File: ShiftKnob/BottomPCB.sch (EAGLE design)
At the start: 37 parts, among them IC2 UA78M05DCY, J1 AVR_SPI_PRG_6PTH, Q1 16MHz, Q2 MOSFET-NCHANNELSMD, Q3 MOSFET-PCHANNELSMD, Q4 MOSFET-NCHANNELSMD, Q5 MOSFET-NCHANNELSMD, Q6 MOSFET-NCHANNELSMD, U1 ATMEGA328, U3 FT232RL-BASICSSOP

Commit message: move silk screens for better visibility.
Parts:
- renumbered U$6 to U6
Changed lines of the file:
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@@
 <part name="GND15" library="SparkFun" deviceset="GND" device=""/>
 <part name="U3" library="SparkFun-DigitalIC" deviceset="FT232RL-BASIC" device="SSOP"/>
-<part name="U$6" library="FORD_frames" deviceset="USB-MINI-B_VERTICAL" device=""/>
+<part name="U6" library="FORD_frames" deviceset="USB-MINI-B_VERTICAL" device=""/>
 <part name="GND20" library="SparkFun" deviceset="GND" device=""/>
 <part name="R13" library="SparkFun" deviceset="RESISTOR" device="0402-RES" value="10K"/>
@@
 <instance part="GND15" gate="1" x="138.43" y="43.18"/>
 <instance part="U3" gate="G$1" x="227.33" y="179.07"/>
-<instance part="U$6" gate="G$1" x="172.72" y="193.04" rot="R180"/>
+<instance part="U6" gate="G$1" x="172.72" y="193.04" rot="R180"/>
 <instance part="GND20" gate="1" x="209.55" y="158.75"/>
 <instance part="R13" gate="G$1" x="256.54" y="184.15" rot="R90"/>
@@
 </segment>
 <segment>
-<pinref part="U$6" gate="G$1" pin="GND"/>
+<pinref part="U6" gate="G$1" pin="GND"/>
 <pinref part="GND11" gate="1" pin="GND"/>
 <wire x1="177.8" y1="196.85" x2="182.88" y2="196.85" width="0.1524" layer="91"/>
@@
 <wire x1="200.66" y1="177.8" x2="200.66" y2="194.31" width="0.1524" layer="91"/>
 <pinref part="C10" gate="G$1" pin="+"/>
-<pinref part="U$6" gate="G$1" pin="VBUS"/>
+<pinref part="U6" gate="G$1" pin="VBUS"/>
 <wire x1="177.8" y1="194.31" x2="189.23" y2="194.31" width="0.1524" layer="91"/>
 <pinref part="U3" gate="G$1" pin="VCC"/>
@@
 <net name="N$21" class="0">
 <segment>
-<pinref part="U$6" gate="G$1" pin="D+"/>
+<pinref part="U6" gate="G$1" pin="D+"/>
 <wire x1="177.8" y1="189.23" x2="212.09" y2="189.23" width="0.1524" layer="91"/>
 <pinref part="U3" gate="G$1" pin="USBDP"/>
@@
 <net name="N$22" class="0">
 <segment>
-<pinref part="U$6" gate="G$1" pin="D-"/>
+<pinref part="U6" gate="G$1" pin="D-"/>
 <wire x1="177.8" y1="191.77" x2="212.09" y2="191.77" width="0.1524" layer="91"/>
 <pinref part="U3" gate="G$1" pin="USBDM"/>

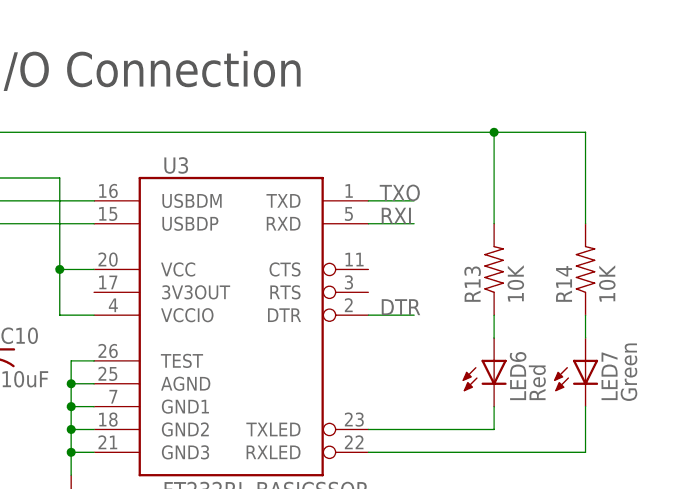
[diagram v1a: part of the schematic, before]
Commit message: fix TX/RX issue on v02 board schematic and layout.
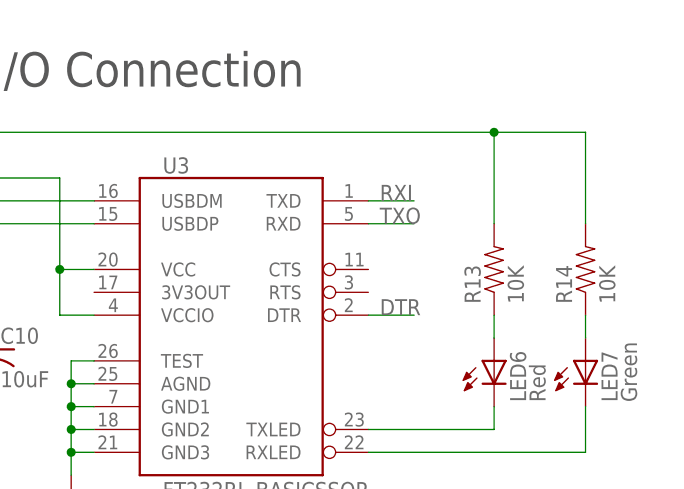
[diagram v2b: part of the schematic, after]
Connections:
- net RXI: now also U3.TXD; no longer U3.RXD
- net TXO: now also U3.RXD; no longer U3.TXD
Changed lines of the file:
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@@
 </segment>
 <segment>
-<wire x1="242.57" y1="191.77" x2="247.65" y2="191.77" width="0.1524" layer="91"/>
-<label x="243.84" y="191.77" size="1.778" layer="95"/>
-<pinref part="U3" gate="G$1" pin="TXD"/>
+<wire x1="242.57" y1="189.23" x2="247.65" y2="189.23" width="0.1524" layer="91"/>
+<label x="243.84" y="189.23" size="1.778" layer="95"/>
+<pinref part="U3" gate="G$1" pin="RXD"/>
 </segment>
 </net>
@@
 </segment>
 <segment>
-<wire x1="242.57" y1="189.23" x2="247.65" y2="189.23" width="0.1524" layer="91"/>
-<label x="243.84" y="189.23" size="1.778" layer="95"/>
-<pinref part="U3" gate="G$1" pin="RXD"/>
-</segment>
-</net>
+<wire x1="242.57" y1="191.77" x2="247.65" y2="191.77" width="0.1524" layer="91"/>
+<label x="243.84" y="191.77" size="1.778" layer="95"/>
+<pinref part="U3" gate="G$1" pin="TXD"/>
+</segment>
+</net>
